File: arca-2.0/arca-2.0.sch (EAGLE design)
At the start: 130 parts, among them IC1 MCP6N11R, IC2 MCP6N11R, IC3 MCP6N11R, IC4 MCP6N11R, IC5 LM324D, SW1 1101M2S3CQE2, T1 FQP30N06L, T2 FQP30N06L, T3 FQP30N06L, T4 FQP30N06L, T5 FQP30N06L, T6 FQP30N06L

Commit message: concept for PTs
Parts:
- removed RZ1, RZ2, RZ3, RZ4: (no value), pot:TRIM_US-S64W
- added C1, C2: (no value), rcl:C-USC1206
- added C20: 0.1u, rcl:C-USC1206
- added CON_PT1: LPTA-2POS, con-phoenix-5mm:LPTA-2POS
- added IC6: LM324D, linear:LM324D
- added R46, R47, R48, R49, R50, R51, R52, R53: 10k, rcl:R-US_R1206
- added R54: 220, rcl:R-US_R1206
- added R55, R56: (no value), rcl:R-US_R1206
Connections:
- removed net +3V3: RZ1.E, RZ2.E, RZ3.E, RZ4.E
- removed net N$22: IC2.REF, RG2.1, RZ2.S
- new net N$2: IC1.REF, R46.1, R47.2, RG1.1
- new net N$37: IC3.REF, R50.1, R51.2, RG3.1
- new net N$38: C1.1, IC6A.+IN, R56.2
- new net PT1-: CON_PT1_2.SK, R54.2, R55.1
- new net PT1_CAL: C2.2, IC6A.-IN, IC6A.OUT
- net +10V_FS: now also CON_PT1_1.SK
- net +5V: now also C20.1, IC6P.V+, R46.2, R48.2, R50.2, R52.2
- net GND: now also C1.2, C20.2, IC6P.V-, R47.1, R49.1, R51.1, R53.1, R54.1; no longer RZ1.A, RZ2.A, RZ3.A, RZ4.A
- net N$17: now also IC2.REF, R48.1, R49.2, RG2.1; no longer IC1.REF, RG1.1, RZ1.S
- net N$25: now also C2.1, R55.2, R56.1; no longer IC3.REF, RG3.1, RZ3.S
- net N$28: now also R52.1, R53.2; no longer RZ4.S
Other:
- note added: "Pressure transducer gives fixed voltage based on pressure. I = 4mA + 16mA/Pmax * P V(PT1-) = 0.00352V/psi * P + 0.88 V"

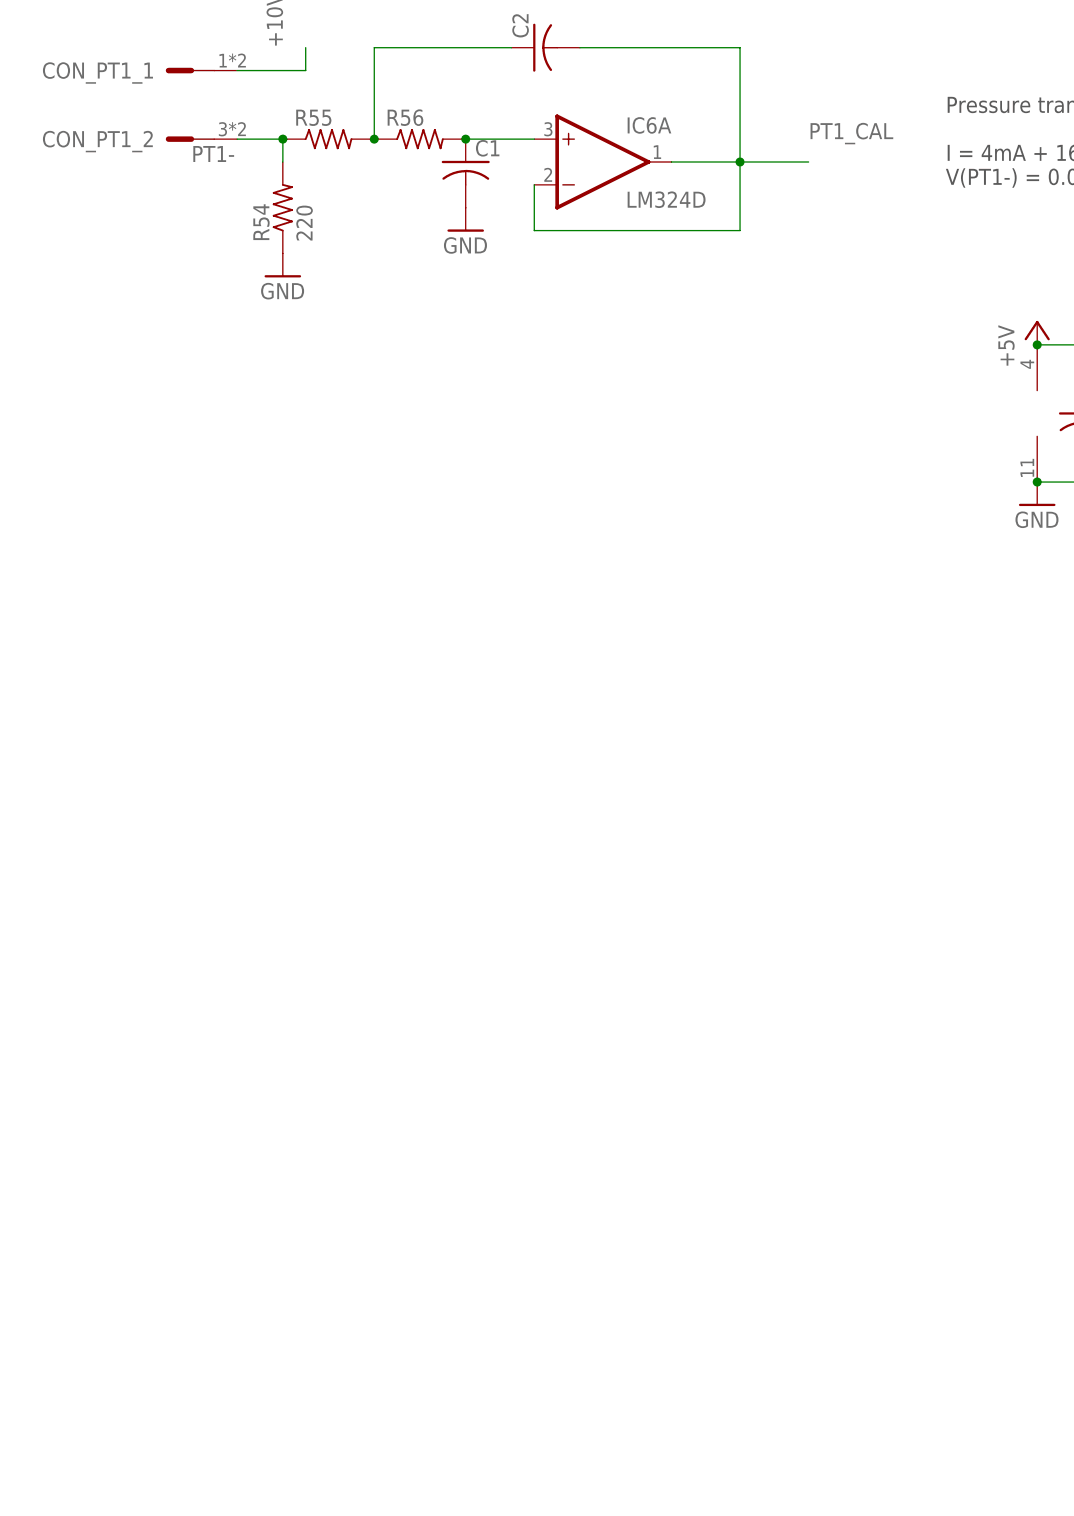
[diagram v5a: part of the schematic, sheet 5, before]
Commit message: now with 10x gain on PTs
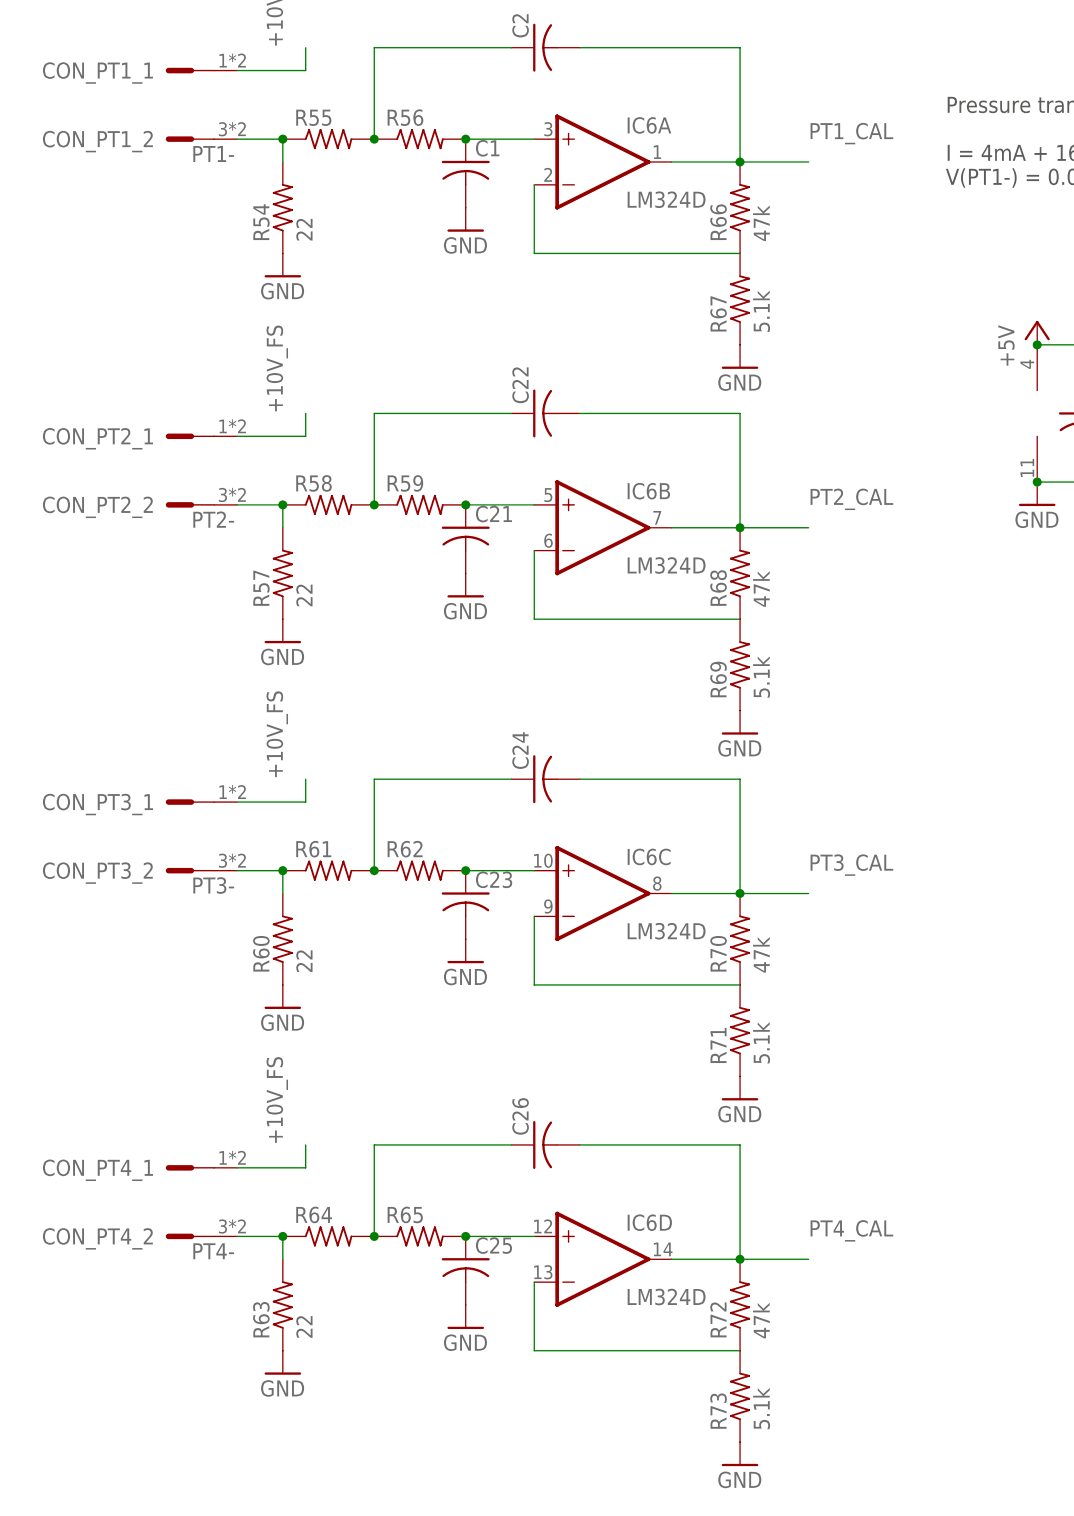
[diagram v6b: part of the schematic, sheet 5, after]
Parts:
- added C21, C22, C23, C24, C25, C26: (no value), rcl:C-USC1206
- added CON_PT2, CON_PT3, CON_PT4: LPTA-2POS, con-phoenix-5mm:LPTA-2POS
- added FS8: 178.6165, fuse-holder-littlefuse:178.6165
- added R57, R60, R63: 22, rcl:R-US_R1206
- added R58, R59, R61, R62, R64, R65: (no value), rcl:R-US_R1206
- added R66, R68, R70, R72: 47k, rcl:R-US_R1206
- added R67, R69, R71, R73: 5.1k, rcl:R-US_R1206
- R54: value 220 -> 22
- RF2, RF3, RF4: value (none) -> 20k
- RG2, RG3, RG4: value (none) -> 200
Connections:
- new net +5V_FS: CON_LC1_1.SK, CON_LC2_1.SK, CON_LC3_1.SK, CON_LC4_1.SK, FS8.1
- new net N$22: C22.1, R58.2, R59.1
- new net N$39: C21.1, IC6B.+IN, R59.2
- new net N$40: C24.1, R61.2, R62.1
- new net N$41: C23.1, IC6C.+IN, R62.2
- new net N$42: C26.1, R64.2, R65.1
- new net N$43: C25.1, IC6D.+IN, R65.2
- new net N$44: IC6D.-IN, R72.1, R73.2
- new net N$45: IC6C.-IN, R70.1, R71.2
- new net N$46: IC6B.-IN, R68.1, R69.2
- new net N$47: IC6A.-IN, R66.1, R67.2
- new net PT2-: CON_PT2_2.SK, R57.2, R58.1
- new net PT2_CAL: C22.2, IC6B.OUT, R68.2
- new net PT3-: CON_PT3_2.SK, R60.2, R61.1
- new net PT3_CAL: C24.2, IC6C.OUT, R70.2
- new net PT4-: CON_PT4_2.SK, R63.2, R64.1
- new net PT4_CAL: C26.2, IC6D.OUT, R72.2
- net +10V_FS: now also CON_PT2_1.SK, CON_PT3_1.SK, CON_PT4_1.SK; no longer CON_LC1_1.SK, CON_LC2_1.SK, CON_LC3_1.SK, CON_LC4_1.SK
- net +5V: now also FS8.2
- net GND: now also C21.2, C23.2, C25.2, R57.1, R60.1, R63.1, R67.1, R69.1, R71.1, R73.1
- net PT1_CAL: now also R66.2; no longer IC6A.-IN

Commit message: updating board with results from data analysis
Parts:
- removed SW1: 1101M2S3CQE2, switch-slide:1101M2S3CQE2
- added CON_FAN: LPTA-2POS, con-phoenix-5mm:LPTA-2POS
- added SW2: 1101M2S3CQE2, switch-slide:1101M2S3CQE2
- C1, C2, C21, C22, C23, C24, C25, C26: value (none) -> 1n
- R25, R29, R33, R37: value 39k -> 15k
- R27, R28: value 56k -> 68k
- R31, R32, R35, R36, R39, R40: value 62k -> 68k
- R55, R56, R58, R59, R61, R62, R64, R65: value (none) -> 68k
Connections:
- new net N$48: CON_FAN_1.SK, SW2.O
- net +12V: now also SW2.P
- net 12V_CON: no longer SW1.P
- net 12V_IN: no longer SW1.O
- net GND: now also CON_FAN_2.SK
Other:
- note added: "Use Bourns CRM1206-FX-22R0ELF (available on mouser) as 22ohm resistor for current sensing"
- note added: "f_c = 2.57 kHz G = 1.5"
- note added: "f_c = 2.57 kHz G = 10.21"
- note removed: "f_c = 2.57 kHz G = 4.9"

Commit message: ADCs now added
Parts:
- added ADC1, ADC2, ADC3: MCP3208SN, microchip-extra:MCP3208SN
- added C27: 0.1u, rcl:C-USC1206
- added R74: 10k, rcl:R-US_R1206
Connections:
- new net N$49: ADC1.CS*, R74.2
- new net SPI_CLK: ADC1.CLK
- new net SPI_MISO: ADC1.DOUT
- new net SPI_MOSI: ADC1.DIN
- net +5V: now also ADC1.VDD, ADC1.VREF, C27.1
- net GND: now also ADC1.AGND, ADC1.DGND, C27.2, R74.1
- net LC1_CAL: now also ADC1.CH0
- net LC2_CAL: now also ADC1.CH1
- net LC3_CAL: now also ADC1.CH2
- net LC4_CAL: now also ADC1.CH3
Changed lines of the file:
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@@
 <part name="GND63" library="supply1" library_urn="urn:adsk.eagle:library:371" deviceset="GND" device=""/>
 <part name="FRAME6" library="frames" library_urn="urn:adsk.eagle:library:229" deviceset="LETTER_L" device=""/>
+<part name="ADC1" library="microchip-extra" deviceset="MCP3208" device="SN"/>
+<part name="ADC2" library="microchip-extra" deviceset="MCP3208" device="SN"/>
+<part name="ADC3" library="microchip-extra" deviceset="MCP3208" device="SN"/>
+<part name="P+25" library="supply1" library_urn="urn:adsk.eagle:library:371" deviceset="+5V" device=""/>
+<part name="GND64" library="supply1" library_urn="urn:adsk.eagle:library:371" deviceset="GND" device=""/>
+<part name="GND65" library="supply1" library_urn="urn:adsk.eagle:library:371" deviceset="GND" device=""/>
+<part name="R74" library="rcl" library_urn="urn:adsk.eagle:library:334" deviceset="R-US_" device="R1206" package3d_urn="urn:adsk.eagle:package:23540/2" value="10k"/>
+<part name="GND66" library="supply1" library_urn="urn:adsk.eagle:library:371" deviceset="GND" device=""/>
+<part name="C27" library="rcl" library_urn="urn:adsk.eagle:library:334" deviceset="C-US" device="C1206" package3d_urn="urn:adsk.eagle:package:23618/2" value="0.1u"/>
 </parts>
 <sheets>
@@
 <attribute name="DRAWING_NAME" x="165.1" y="19.05" size="2.54" layer="94"/>
 </instance>
+<instance part="ADC1" gate="P" x="53.34" y="154.94" smashed="yes">
+<attribute name="NAME" x="43.18" y="171.45" size="1.778" layer="95"/>
+<attribute name="VALUE" x="43.18" y="137.16" size="1.778" layer="96"/>
+</instance>
+<instance part="ADC2" gate="P" x="53.34" y="109.22" smashed="yes">
+<attribute name="NAME" x="43.18" y="125.73" size="1.778" layer="95"/>
+<attribute name="VALUE" x="43.18" y="91.44" size="1.778" layer="96"/>
+</instance>
+<instance part="ADC3" gate="P" x="53.34" y="60.96" smashed="yes">
+<attribute name="NAME" x="43.18" y="77.47" size="1.778" layer="95"/>
+<attribute name="VALUE" x="43.18" y="43.18" size="1.778" layer="96"/>
+</instance>
+<instance part="P+25" gate="1" x="68.58" y="175.26" smashed="yes">
+<attribute name="VALUE" x="66.04" y="170.18" size="1.778" layer="96" rot="R90"/>
+</instance>
+<instance part="GND64" gate="1" x="38.1" y="137.16" smashed="yes">
+<attribute name="VALUE" x="35.56" y="134.62" size="1.778" layer="96"/>
+</instance>
+<instance part="GND65" gate="1" x="68.58" y="154.94" smashed="yes">
+<attribute name="VALUE" x="71.12" y="154.94" size="1.778" layer="96"/>
+</instance>
+<instance part="R74" gate="G$1" x="71.12" y="137.16" smashed="yes" rot="R90">
+<attribute name="NAME" x="69.6214" y="133.35" size="1.778" layer="95" rot="R90"/>
+<attribute name="VALUE" x="74.422" y="133.35" size="1.778" layer="96" rot="R90"/>
+</instance>
+<instance part="GND66" gate="1" x="71.12" y="129.54" smashed="yes">
+<attribute name="VALUE" x="68.58" y="127" size="1.778" layer="96"/>
+</instance>
+<instance part="C27" gate="G$1" x="73.66" y="165.1" smashed="yes">
+<attribute name="NAME" x="74.676" y="165.735" size="1.778" layer="95"/>
+<attribute name="VALUE" x="74.676" y="160.909" size="1.778" layer="96"/>
+</instance>
 </instances>
 <busses>
 </busses>
 <nets>
+<net name="LC1_CAL" class="0">
+<segment>
+<pinref part="ADC1" gate="P" pin="CH0"/>
+<wire x1="40.64" y1="167.64" x2="27.94" y2="167.64" width="0.1524" layer="91"/>
+<label x="27.94" y="167.64" size="1.778" layer="95"/>
+</segment>
+</net>
+<net name="LC2_CAL" class="0">
+<segment>
+<pinref part="ADC1" gate="P" pin="CH1"/>
+<wire x1="40.64" y1="165.1" x2="27.94" y2="165.1" width="0.1524" layer="91"/>
+<label x="27.94" y="165.1" size="1.778" layer="95"/>
+</segment>
+</net>
+<net name="LC3_CAL" class="0">
+<segment>
+<pinref part="ADC1" gate="P" pin="CH2"/>
+<wire x1="40.64" y1="162.56" x2="27.94" y2="162.56" width="0.1524" layer="91"/>
+<label x="27.94" y="162.56" size="1.778" layer="95"/>
+</segment>
+</net>
+<net name="LC4_CAL" class="0">
+<segment>
+<pinref part="ADC1" gate="P" pin="CH3"/>
+<wire x1="40.64" y1="160.02" x2="27.94" y2="160.02" width="0.1524" layer="91"/>
+<label x="27.94" y="160.02" size="1.778" layer="95"/>
+</segment>
+</net>
+<net name="+5V" class="3">
+<segment>
+<pinref part="P+25" gate="1" pin="+5V"/>
+<wire x1="68.58" y1="172.72" x2="68.58" y2="167.64" width="0.1524" layer="91"/>
+<pinref part="ADC1" gate="P" pin="VREF"/>
+<wire x1="68.58" y1="167.64" x2="68.58" y2="162.56" width="0.1524" layer="91"/>
+<wire x1="68.58" y1="162.56" x2="66.04" y2="162.56" width="0.1524" layer="91"/>
+<pinref part="ADC1" gate="P" pin="VDD"/>
+<wire x1="66.04" y1="167.64" x2="68.58" y2="167.64" width="0.1524" layer="91"/>
+<junction x="68.58" y="167.64"/>
+<pinref part="C27" gate="G$1" pin="1"/>
+<wire x1="73.66" y1="167.64" x2="68.58" y2="167.64" width="0.1524" layer="91"/>
+</segment>
+</net>
+<net name="GND" class="0">
+<segment>
+<pinref part="ADC1" gate="P" pin="AGND"/>
+<pinref part="GND65" gate="1" pin="GND"/>
+<wire x1="66.04" y1="157.48" x2="68.58" y2="157.48" width="0.1524" layer="91"/>
+<wire x1="68.58" y1="157.48" x2="73.66" y2="157.48" width="0.1524" layer="91"/>
+<pinref part="C27" gate="G$1" pin="2"/>
+<wire x1="73.66" y1="157.48" x2="73.66" y2="160.02" width="0.1524" layer="91"/>
+<junction x="68.58" y="157.48"/>
+</segment>
+<segment>
+<pinref part="R74" gate="G$1" pin="1"/>
+<pinref part="GND66" gate="1" pin="GND"/>
+</segment>
+<segment>
+<pinref part="ADC1" gate="P" pin="DGND"/>
+<wire x1="40.64" y1="142.24" x2="38.1" y2="142.24" width="0.1524" layer="91"/>
+<pinref part="GND64" gate="1" pin="GND"/>
+<wire x1="38.1" y1="142.24" x2="38.1" y2="139.7" width="0.1524" layer="91"/>
+</segment>
+</net>
+<net name="SPI_CLK" class="0">
+<segment>
+<pinref part="ADC1" gate="P" pin="CLK"/>
+<wire x1="66.04" y1="152.4" x2="81.28" y2="152.4" width="0.1524" layer="91"/>
+<label x="81.28" y="152.4" size="1.778" layer="95"/>
+</segment>
+</net>
+<net name="N$49" class="0">
+<segment>
+<pinref part="ADC1" gate="P" pin="CS*"/>
+<pinref part="R74" gate="G$1" pin="2"/>
+<wire x1="66.04" y1="142.24" x2="71.12" y2="142.24" width="0.1524" layer="91"/>
+</segment>
+</net>
+<net name="SPI_MISO" class="0">
+<segment>
+<pinref part="ADC1" gate="P" pin="DOUT"/>
+<wire x1="66.04" y1="147.32" x2="81.28" y2="147.32" width="0.1524" layer="91"/>
+<label x="81.28" y="147.32" size="1.778" layer="95"/>
+</segment>
+</net>
+<net name="SPI_MOSI" class="0">
+<segment>
+<pinref part="ADC1" gate="P" pin="DIN"/>
+<wire x1="66.04" y1="144.78" x2="81.28" y2="144.78" width="0.1524" layer="91"/>
+<label x="81.28" y="144.78" size="1.778" layer="95"/>
+</segment>
+</net>
 </nets>
 </sheet>
